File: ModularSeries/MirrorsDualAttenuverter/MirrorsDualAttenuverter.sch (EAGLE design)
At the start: 33 parts, among them IC2 LM358

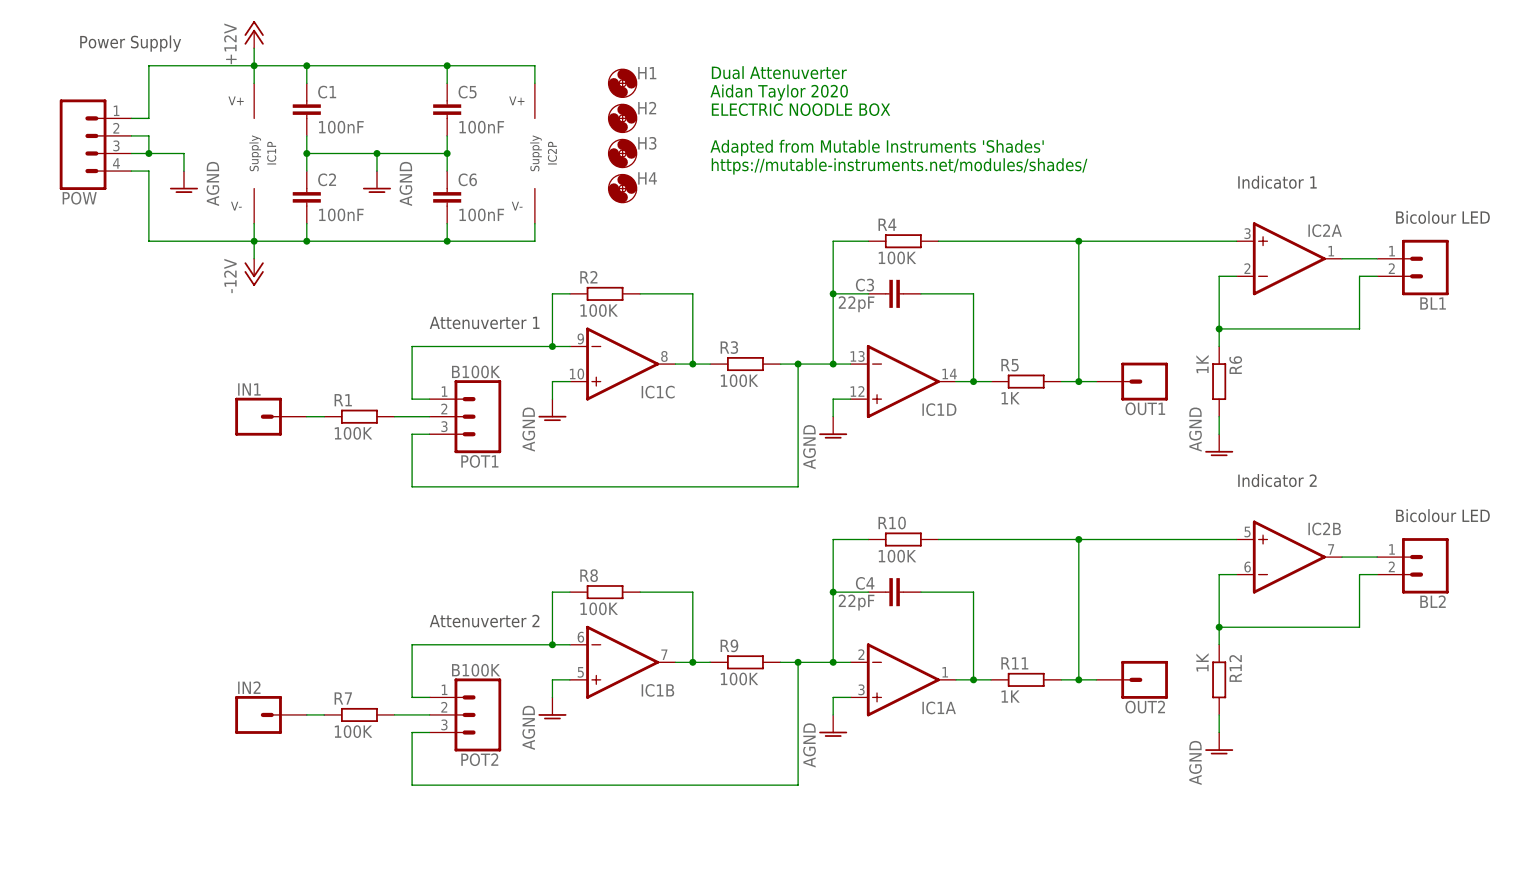
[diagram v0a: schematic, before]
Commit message: Mirrors Dual Attenuverter DC offset added, layout updated
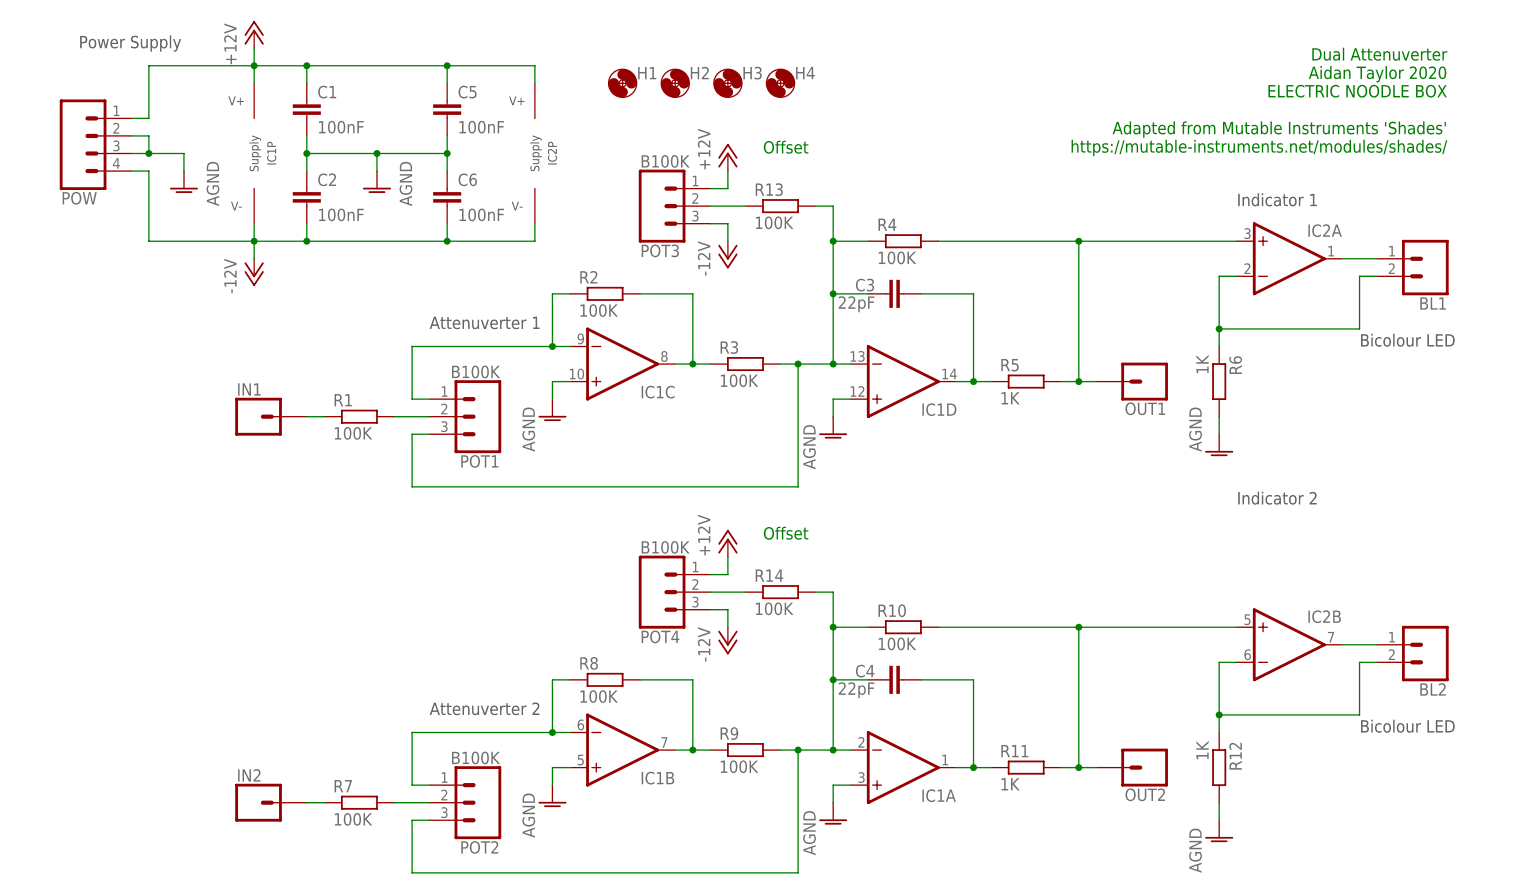
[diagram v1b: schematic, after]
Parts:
- added POT3, POT4: B100K, ElectricNoodleBox:3XWIREPAD
- added R13, R14: 100K, rcl:R-EU_0207/10
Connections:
- new net N$20: POT3.2, R13.1
- new net N$22: POT4.2, R14.1
- net +12V: now also POT3.1, POT4.1
- net -12V: now also POT3.3, POT4.3
- net N$13: now also R14.2
- net N$5: now also R13.2
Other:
- note added: "Offset"
- moved on the sheet: BL2, C4, H2, H3, H4, IC1A, IC1B, IC2B, IN2, OUT2, POT2, R10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

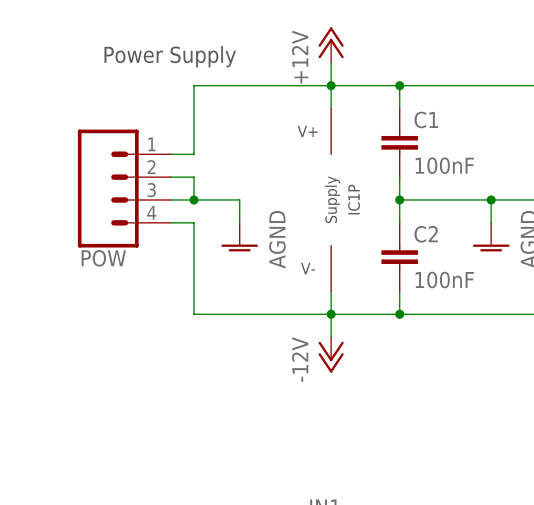
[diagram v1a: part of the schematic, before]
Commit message: Power header updated on most PCBs. Knives layout added
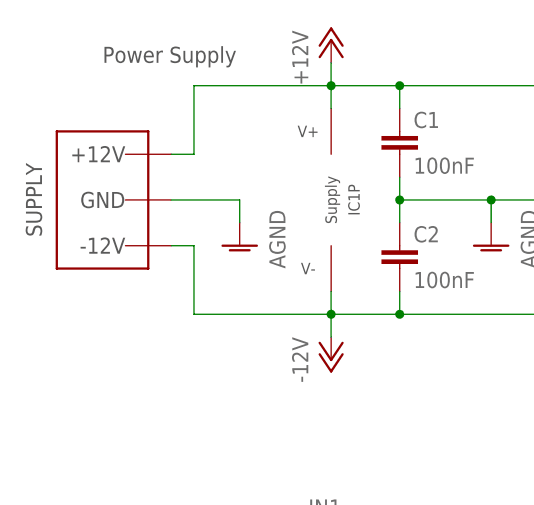
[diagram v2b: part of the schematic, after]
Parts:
- removed POW: 4XMOLEX, ElectricNoodleBox:4XMOLEX
- added WP1: COMBO_SUPPLY_HEADER, ElectricNoodleBox:COMBO_SUPPLY_HEADER
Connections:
- net +12V: now also WP1.V++; no longer POW.1
- net -12V: now also WP1.V--; no longer POW.4
- net AGND: now also WP1.AGND; no longer POW.2, POW.3
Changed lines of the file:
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@@
 <part name="H3" library="holes" library_urn="urn:adsk.eagle:library:237" deviceset="MOUNT-HOLE" device="3.2" package3d_urn="urn:adsk.eagle:package:14275/1"/>
 <part name="H4" library="holes" library_urn="urn:adsk.eagle:library:237" deviceset="MOUNT-HOLE" device="3.2" package3d_urn="urn:adsk.eagle:package:14275/1"/>
-<part name="POW" library="ElectricNoodleBox" deviceset="4XMOLEX" device=""/>
 <part name="AGND8" library="supply1" library_urn="urn:adsk.eagle:library:371" deviceset="AGND" device=""/>
 <part name="POT1" library="ElectricNoodleBox" deviceset="3XWIREPAD" device="" value="B100K"/>
@@
 <part name="P-3" library="supply1" library_urn="urn:adsk.eagle:library:371" deviceset="-12V" device=""/>
 <part name="R14" library="rcl" library_urn="urn:adsk.eagle:library:334" deviceset="R-EU_" device="0207/10" package3d_urn="urn:adsk.eagle:package:23491/2" value="100K"/>
+<part name="WP1" library="ElectricNoodleBox" deviceset="COMBO_SUPPLY_HEADER" device=""/>
 </parts>
 <sheets>
@@
 <attribute name="NAME" x="85.852" y="107.2642" size="1.778" layer="95"/>
 </instance>
-<instance part="POW" gate="G$1" x="-15.24" y="99.06" smashed="yes" rot="MR180">
-<attribute name="NAME" x="-20.32" y="90.932" size="1.778" layer="95" font="vector" rot="MR180"/>
-</instance>
 <instance part="AGND8" gate="VR1" x="-2.54" y="91.44" smashed="yes">
 <attribute name="VALUE" x="2.54" y="88.9" size="1.778" layer="96" rot="R90"/>
@@
 <attribute name="VALUE" x="80.01" y="29.718" size="1.778" layer="96"/>
 </instance>
+<instance part="WP1" gate="G$1" x="-17.78" y="96.52" smashed="yes" rot="MR0"/>
 </instances>
 <busses>
@@
 </segment>
 <segment>
-<pinref part="POW" gate="G$1" pin="3"/>
-<wire x1="-10.16" y1="96.52" x2="-7.62" y2="96.52" width="0.1524" layer="91"/>
 <pinref part="AGND8" gate="VR1" pin="AGND"/>
-<wire x1="-7.62" y1="96.52" x2="-2.54" y2="96.52" width="0.1524" layer="91"/>
+<wire x1="-10.16" y1="96.52" x2="-2.54" y2="96.52" width="0.1524" layer="91"/>
 <wire x1="-2.54" y1="96.52" x2="-2.54" y2="93.98" width="0.1524" layer="91"/>
-<pinref part="POW" gate="G$1" pin="2"/>
-<wire x1="-10.16" y1="99.06" x2="-7.62" y2="99.06" width="0.1524" layer="91"/>
-<wire x1="-7.62" y1="99.06" x2="-7.62" y2="96.52" width="0.1524" layer="91"/>
-<junction x="-7.62" y="96.52"/>
+<pinref part="WP1" gate="G$1" pin="AGND"/>
 </segment>
 </net>
@@
 <wire x1="15.24" y1="109.22" x2="15.24" y2="106.68" width="0.1524" layer="91"/>
 <junction x="15.24" y="109.22"/>
-<pinref part="POW" gate="G$1" pin="1"/>
 <wire x1="-10.16" y1="101.6" x2="-7.62" y2="101.6" width="0.1524" layer="91"/>
 <wire x1="-7.62" y1="101.6" x2="-7.62" y2="109.22" width="0.1524" layer="91"/>
@@
 <pinref part="IC2" gate="P" pin="V+"/>
 <wire x1="48.26" y1="109.22" x2="48.26" y2="106.68" width="0.1524" layer="91"/>
+<pinref part="WP1" gate="G$1" pin="V++"/>
 </segment>
 <segment>
@@
 <wire x1="15.24" y1="86.36" x2="15.24" y2="83.82" width="0.1524" layer="91"/>
 <junction x="15.24" y="83.82"/>
-<pinref part="POW" gate="G$1" pin="4"/>
-<wire x1="-10.16" y1="93.98" x2="-7.62" y2="93.98" width="0.1524" layer="91"/>
-<wire x1="-7.62" y1="93.98" x2="-7.62" y2="83.82" width="0.1524" layer="91"/>
+<wire x1="-10.16" y1="91.44" x2="-7.62" y2="91.44" width="0.1524" layer="91"/>
+<wire x1="-7.62" y1="91.44" x2="-7.62" y2="83.82" width="0.1524" layer="91"/>
 <wire x1="-7.62" y1="83.82" x2="7.62" y2="83.82" width="0.1524" layer="91"/>
 <pinref part="IC2" gate="P" pin="V-"/>
 <wire x1="48.26" y1="83.82" x2="48.26" y2="86.36" width="0.1524" layer="91"/>
-</segment>
-<segment>
+<pinref part="WP1" gate="G$1" pin="V--"/>
+</segment>
+<segment>
